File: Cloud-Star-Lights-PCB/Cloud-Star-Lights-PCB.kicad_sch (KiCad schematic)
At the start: 79 parts, among them U1 RP2040, U2 PCA9685PW, U3 PCA9685PW

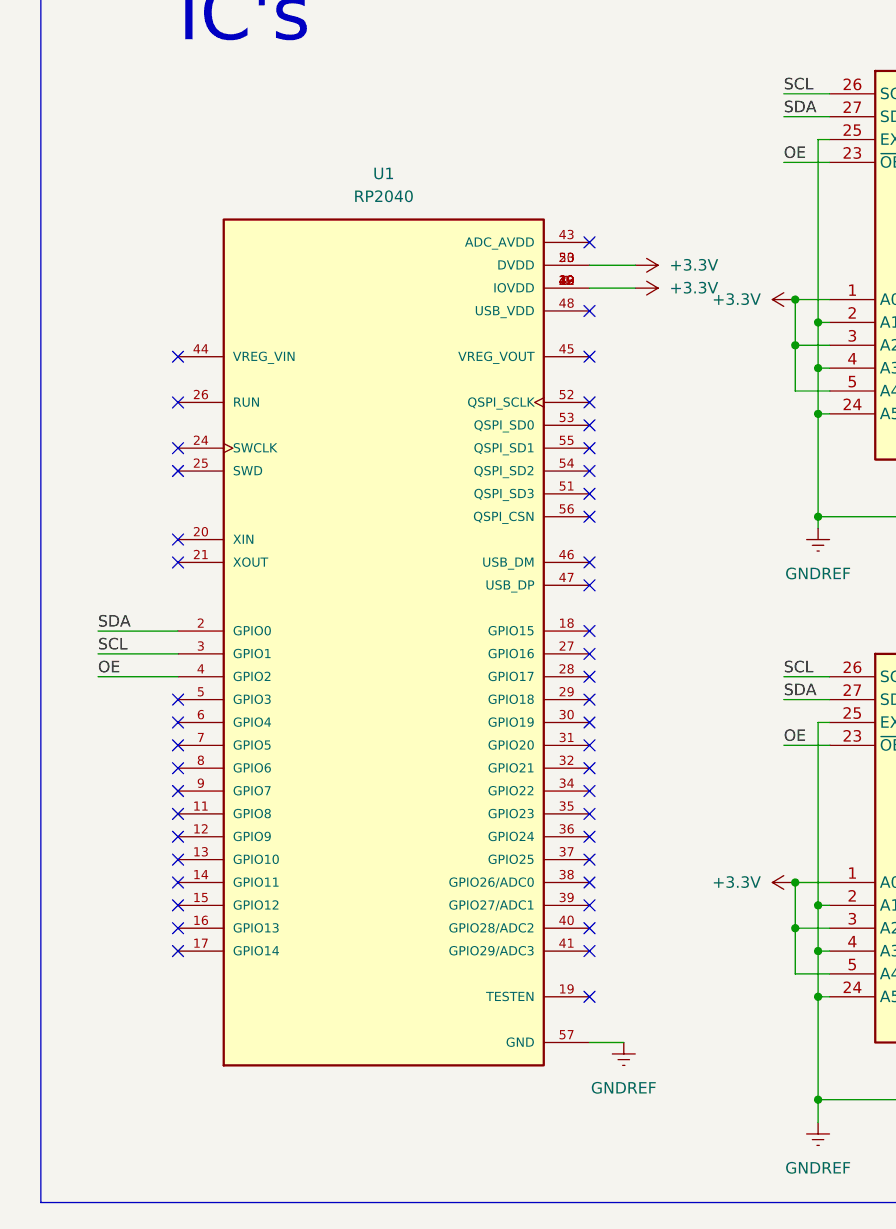
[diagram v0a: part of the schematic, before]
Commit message: Convert to ESP chip and localize library (hopefully)
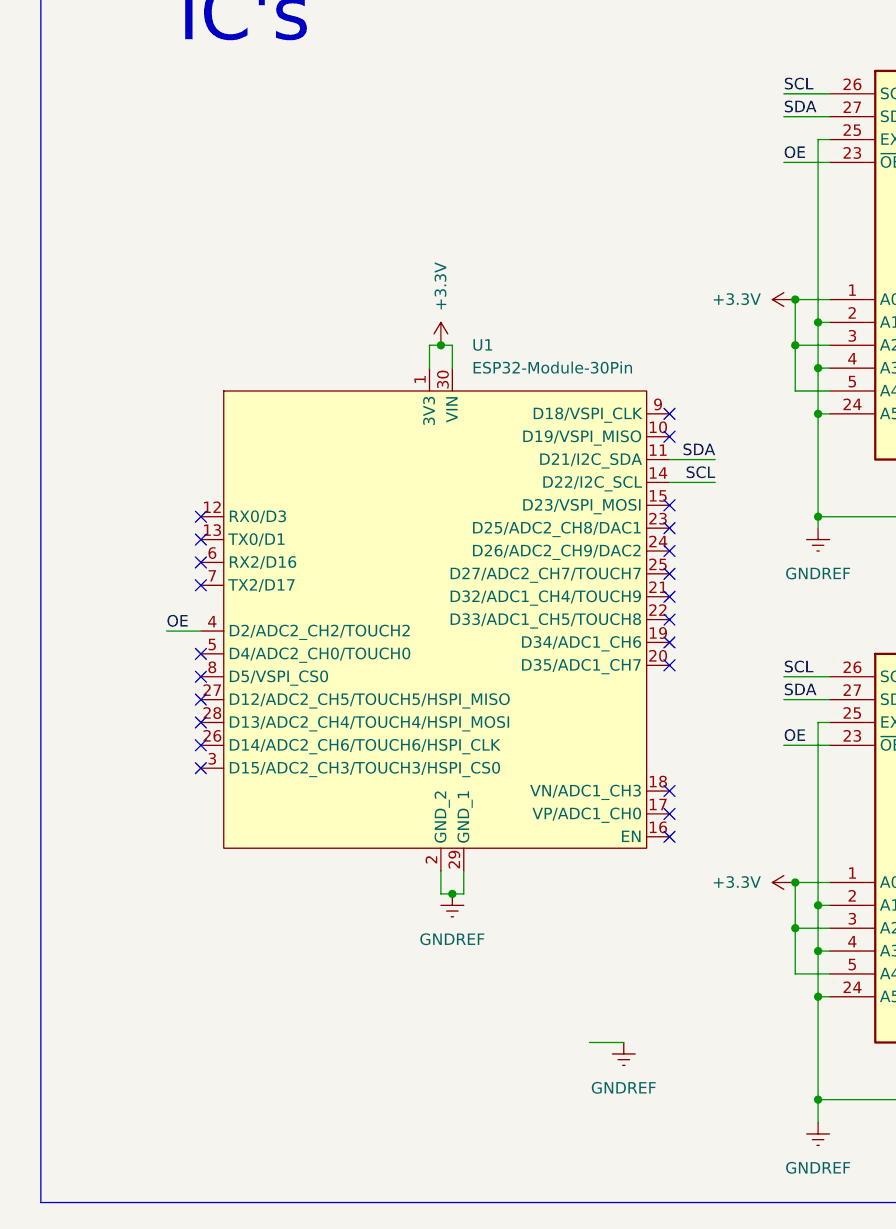
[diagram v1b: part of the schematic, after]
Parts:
- removed U1: RP2040, RP2040:QFN40P700X700X90-57N, symbol RP2040:RP2040
- added U1: ESP32-Module-30Pin, Project-Supernova-Footprint-Lib:ESP32-Module-30Pin, symbol Library:ESP32-Module-30Pin
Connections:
- net +3.3V: now also U1.1 (3V3), U1.30 (VIN)
- net GNDREF: now also U1.2 (GND_2), U1.29 (GND_1)
- net OE: now also U1.4 (D2/ADC2_CH2/TOUCH2)
- net SCL: now also U1.14 (D22/I2C_SCL)
- net SDA: now also U1.11 (D21/I2C_SDA)
- no-connect marks 47 -> 25

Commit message: Praying to god my library is right
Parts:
- J1, J10, J11, J12, J13, J14, J15, J16, J17, J18, J19, J2, J20, J21, J22, J23, J24, J25, J26, J27, J28, J29, J3, J30, J31, J32, J33, J34, J35, J36, J37, J38, J39, J4, J40, J41, J42, J43, J44, J45, J5, J6, J7, J8, J9: footprint (none) -> Library:0353120460
- J46: footprint (none) -> Library:Cixi_Kefa_Elec_KF135T-10.16-3P
- Q1, Q10, Q11, Q12, Q13, Q14, Q15, Q16, Q17, Q18, Q19, Q2, Q20, Q21, Q22, Q23, Q24, Q25, Q26, Q27, Q28, Q29, Q3, Q30, Q4, Q5, Q6, Q7, Q8, Q9: footprint (none) -> Library:AP5N10S
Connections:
- net OE: now also U1.15 (D23/VSPI_MOSI); no longer U1.4 (D2/ADC2_CH2/TOUCH2)

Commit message: Schematics Done
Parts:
- removed J1, J10, J11, J12, J13, J14, J15, J16, J17, J18, J19, J2, J20, J21, J22, J23, J24, J25, J26, J27, J28, J29, J3, J30, J31, J32, J33, J34, J35, J36, J37, J38, J39, J4, J40, J41, J42, J43, J44, J45, J5, J6, J7, J8, J9: ~, Library:0353120460, symbol Library:0353120460
- removed Q1, Q10, Q11, Q12, Q13, Q14, Q15, Q16, Q17, Q18, Q19, Q2, Q20, Q21, Q22, Q23, Q24, Q25, Q26, Q27, Q28, Q29, Q3, Q4, Q5, Q6, Q7, Q8, Q9: ~, Library:AP5N10S, symbol Library:AP5N10S
- added J1, J32, J33, J34, J35, J36, J37, J38, J39, J40, J41, J42, J43, J44, J45: ~, symbol Library:JILN_JL301-50004U01
- added J10, J11, J12, J13, J14, J15, J16, J17, J18, J19, J2, J20, J21, J22, J23, J24, J25, J26, J27, J28, J29, J3, J30, J31, J4, J5, J6, J7, J8, J9: ~, symbol Library:MAX_MX126-5.0-02P-GN01-Cu-S-A
- added Q1, Q10, Q11, Q12, Q13, Q14, Q15, Q16, Q17, Q18, Q19, Q2, Q20, Q21, Q22, Q23, Q24, Q25, Q26, Q27, Q28, Q29, Q3, Q31, Q4, Q5, Q6, Q7, Q8, Q9: 2N3906, Package_TO_SOT_THT:TO-92_Inline, symbol Transistor_BJT:2N3906
- added Q32, Q33, Q34, Q35, Q36, Q37, Q38, Q39, Q40, Q41, Q42, Q43, Q44, Q45, Q46, Q47, Q48, Q49, Q50, Q51, Q52, Q53, Q54, Q55, Q56, Q57, Q58, Q59, Q60, Q61, Q62, Q63, Q64, Q65, Q66, Q67, Q68, Q69, Q70, Q71, Q72, Q73, Q74, Q75: ~, Library:AP5N10S, symbol Library:AP5N10S
- added R1, R10, R11, R12, R13, R14, R15, R16, R17, R18, R19, R2, R20, R21, R22, R23, R24, R25, R26, R27, R28, R29, R3, R30, R4, R5, R6, R7, R8, R9: ~, Resistor_SMD:R_0201_0603Metric_Pad0.64x0.40mm_HandSolder, symbol Library:ERJP03J220V
- added U4: PCA9685PW, Package_SO:TSSOP-28_4.4x9.7mm_P0.65mm, symbol Driver_LED:PCA9685PW
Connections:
- net Stars_Power_B5 is gone; now on net Cloud_Control_R1: Q30.1 (B)
- net +3.3V: now also U4.1 (A0), U4.24 (A5), U4.28 (VDD), U4.3 (A2); no longer U3.5 (A4)
- net +5V: now also J1.4, J32.4, J33.4, J34.4, J35.4, J36.4, J37.4, J38.4, J39.4, J40.4, J41.4, J42.4, J43.4, J44.4, J45.4, Q1.1 (E), Q10.1 (E), Q11.1 (E), Q12.1 (E), Q13.1 (E), Q14.1 (E), Q15.1 (E), Q16.1 (E), Q17.1 (E), Q18.1 (E), Q19.1 (E), Q2.1 (E), Q20.1 (E), Q21.1 (E), Q22.1 (E), Q23.1 (E), Q24.1 (E), Q25.1 (E), Q26.1 (E), Q27.1 (E), Q28.1 (E), Q29.1 (E), Q3.1 (E), Q31.1 (E), Q4.1 (E), Q5.1 (E), Q6.1 (E), Q7.1 (E), Q8.1 (E), Q9.1 (E)
- net GNDREF: now also Q30.3 (E), U3.5 (A4), J10.2, J11.2, J12.2, J13.2, J14.2, J15.2, J16.2, J17.2, J18.2, J19.2, J2.2, J20.2, J21.2, J22.2, J23.2, J24.2, J25.2, J26.2, J27.2, J28.2, J29.2, J3.2, J30.2, J31.2, J4.2, J5.2, J6.2, J7.2, J8.2, J9.2, Q32.3 (E), Q33.3 (E), Q34.3 (E), Q35.3 (E), Q36.3 (E), Q37.3 (E), Q38.3 (E), Q39.3 (E), Q40.3 (E), Q41.3 (E), Q42.3 (E), Q43.3 (E), Q44.3 (E), Q45.3 (E), Q46.3 (E), Q47.3 (E), Q48.3 (E), Q49.3 (E), Q50.3 (E), Q51.3 (E), Q52.3 (E), Q53.3 (E), Q54.3 (E), Q55.3 (E), Q56.3 (E), Q57.3 (E), Q58.3 (E), Q59.3 (E), Q60.3 (E), Q61.3 (E), Q62.3 (E), Q63.3 (E), Q64.3 (E), Q65.3 (E), Q66.3 (E), Q67.3 (E), Q68.3 (E), Q69.3 (E), Q70.3 (E), Q71.3 (E), Q72.3 (E), Q73.3 (E), Q74.3 (E), Q75.3 (E), U4.14 (VSS), U4.2 (A1), U4.25 (EXTCLK), U4.4 (A3), U4.5 (A4); no longer Q30.1 (E)
- net OE: now also U4.23 (~{OE})
- net SCL: now also U4.26 (SCL)
- net SDA: now also U4.27 (SDA)
- net Clouds_Control_B1 renamed Star_Control_3
- net Star_Control_3: now also Q2.2 (B)
- net Clouds_Control_B2 renamed Star_Control_6
- net Star_Control_6: now also Q5.2 (B)
- net Clouds_Control_B3 renamed Star_Control_9
- net Star_Control_9: now also Q8.2 (B)
- net Clouds_Control_B4 renamed Star_Control_12
- net Star_Control_12: now also Q11.2 (B)
- net Clouds_Control_B5 renamed Star_Control_15
- net Star_Control_15: now also Q14.2 (B)
- net Clouds_Control_G1 renamed Star_Control_2
- net Star_Control_2: now also Q1.2 (B)
- net Clouds_Control_G2 renamed Star_Control_5
- net Star_Control_5: now also Q4.2 (B)
- net Clouds_Control_G3 renamed Star_Control_8
- net Star_Control_8: now also Q7.2 (B)
- net Clouds_Control_G4 renamed Star_Control_11
- net Star_Control_11: now also Q10.2 (B)
- net Clouds_Control_G5 renamed Star_Control_14
- net Star_Control_14: now also Q13.2 (B)
- net Clouds_Control_R1 renamed Star_Control_1
- net Star_Control_1: now also Q31.2 (B)
- net Clouds_Control_R2 renamed Star_Control_4
- net Star_Control_4: now also Q3.2 (B)
- net Clouds_Control_R3 renamed Star_Control_7
- net Star_Control_7: now also Q6.2 (B)
- net Clouds_Control_R4 renamed Star_Control_10
- net Star_Control_10: now also Q9.2 (B)
- net Clouds_Control_R5 renamed Star_Control_13
- net Star_Control_13: now also Q12.2 (B)
- net Stars_Control_B1 renamed Star_Control_18
- net Star_Control_18: now also Q17.2 (B)
- net Stars_Control_B2 renamed Star_Control_21
- net Star_Control_21: now also Q20.2 (B)
- net Stars_Control_B3 renamed Star_Control_24
- net Star_Control_24: now also Q23.2 (B)
- net Stars_Control_B4 renamed Star_Control_27
- net Star_Control_27: now also Q26.2 (B)
- net Stars_Control_B5 renamed Cloud_Control_R1
- net Cloud_Control_R1: now also Q34.1 (B), Q37.1 (B), U4.6 (LED0); no longer U3.21 (LED14)
- net Stars_Control_G1 renamed Star_Control_17
- net Star_Control_17: now also Q16.2 (B)
- net Stars_Control_G2 renamed Star_Control_20
- net Star_Control_20: now also Q19.2 (B)
- net Stars_Control_G3 renamed Star_Control_23
- net Star_Control_23: now also Q22.2 (B)
- net Stars_Control_G4 renamed Star_Control_26
- net Star_Control_26: now also Q25.2 (B)
- net Stars_Control_G5 renamed Star_Control_29
- net Star_Control_29: now also Q28.2 (B)
- net Stars_Control_R1 renamed Star_Control_16
- net Star_Control_16: now also Q15.2 (B)
- net Stars_Control_R2 renamed Star_Control_19
- net Star_Control_19: now also Q18.2 (B)
- net Stars_Control_R3 renamed Star_Control_22
- net Star_Control_22: now also Q21.2 (B)
- net Stars_Control_R4 renamed Star_Control_25
- net Star_Control_25: now also Q24.2 (B)
- net Stars_Control_R5 renamed Star_Control_28
- net Star_Control_28: now also Q27.2 (B)
- new net: J41.1, Q61.2 (C)
- new net: J41.2, Q62.2 (C)
- new net: J41.3, Q63.2 (C)
- new net: J2.1, R1.2
- new net: Q14.3 (C), R15.1
- new net: J16.1, R15.2
- new net: J43.1, Q67.2 (C)
- new net: J43.2, Q68.2 (C)
- new net: J43.3, Q69.2 (C)
- new net: Q13.3 (C), R14.1
- new net: J15.1, R14.2
- new net: J37.1, Q49.2 (C)
- new net: Q19.3 (C), R20.1
- new net: J21.1, R20.2
- new net: J37.3, Q51.2 (C)
- new net: Q2.3 (C), R3.1
- new net: J4.1, R3.2
- new net: Q29.3 (C), R30.1
- new net: J31.1, R30.2
- new net: Q18.3 (C), R19.1
- new net: J20.1, R19.2
- new net: J22.1, R21.2
- new net: J25.1, R24.2
- new net: Q21.3 (C), R22.1
- new net: J23.1, R22.2
- new net: J18.1, R17.2
- new net: J13.1, R12.2
- new net: Q20.3 (C), R21.1
- new net: Q28.3 (C), R29.1
- new net: J42.2, Q65.2 (C)
- new net: Q26.3 (C), R27.1
- new net: J28.1, R27.2
- new net: Q16.3 (C), R17.1
- new net: J35.1, Q43.2 (C)
- new net: J32.3, Q36.2 (C)
- new net: J34.1, Q40.2 (C)
- new net: J39.1, Q55.2 (C)
- new net: J39.2, Q56.2 (C)
- new net: J39.3, Q57.2 (C)
- new net: Q10.3 (C), R11.1
- new net: J12.1, R11.2
- new net: Q1.3 (C), R2.1
- new net: J3.1, R2.2
- new net: J37.2, Q50.2 (C)
- new net: J14.1, R13.2
- new net: J5.1, R4.2
- new net: J1.2, Q32.2 (C)
- new net: J32.1, Q34.2 (C)
- new net: J32.2, Q35.2 (C)
- new net: Q15.3 (C), R16.1
- new net: Q7.3 (C), R8.1
- new net: J9.1, R8.2
- new net: J33.2, Q38.2 (C)
- new net: J8.1, R7.2
- new net: J33.1, Q37.2 (C)
- new net: J33.3, Q39.2 (C)
- new net: J27.1, R26.2
- new net: Q12.3 (C), R13.1
- new net: J34.3, Q42.2 (C)
- new net: J44.2, Q71.2 (C)
- new net: J38.2, Q53.2 (C)
- new net: Q4.3 (C), R5.1
- new net: Q5.3 (C), R6.1
- new net: J38.3, Q54.2 (C)
- new net: J45.1, Q73.2 (C)
- new net: J45.2, Q74.2 (C)
- new net: J45.3, Q75.2 (C)
- new net: Q11.3 (C), R12.1
- new net: J6.1, R5.2
- new net: J38.1, Q52.2 (C)
- new net: Q22.3 (C), R23.1
- new net: J24.1, R23.2
- new net: Q9.3 (C), R10.1
- new net: J36.2, Q47.2 (C)
- new net: J19.1, R18.2
- new net: J30.1, R29.2
- new net: J40.2, Q59.2 (C)
- new net: Q17.3 (C), R18.1
- new net: J35.3, Q45.2 (C)
- new net: J42.3, Q66.2 (C)
- new net: Q8.3 (C), R9.1
- new net: J10.1, R9.2
- new net: J17.1, R16.2
- new net: J44.1, Q70.2 (C)
- new net: J34.2, Q41.2 (C)
- new net: J1.3, Q33.2 (C)
- new net: Q27.3 (C), R28.1
- new net: J29.1, R28.2
- new net: Q3.3 (C), R4.1
- new net: J26.1, R25.2
- new net: Q24.3 (C), R25.1
- new net: J35.2, Q44.2 (C)
- new net: Q6.3 (C), R7.1
- new net: J40.1, Q58.2 (C)
- new net: J40.3, Q60.2 (C)
- new net: Q31.3 (C), R1.1
- new net: J7.1, R6.2
- new net: Q25.3 (C), R26.1
- new net: Q23.3 (C), R24.1
- new net: J1.1, Q30.2 (C)
- new net: J42.1, Q64.2 (C)
- new net: J11.1, R10.2
- new net: J36.3, Q48.2 (C)
- new net: J36.1, Q46.2 (C)
- new net: J44.3, Q72.2 (C)
- new net Cloud_Control_B1: Q33.1 (B), Q36.1 (B), Q39.1 (B), U4.17 (LED10)
- new net Cloud_Control_B2: Q42.1 (B), Q54.1 (B), Q66.1 (B), U4.18 (LED11)
- new net Cloud_Control_B3: Q45.1 (B), Q57.1 (B), Q69.1 (B), U4.19 (LED12)
- new net Cloud_Control_B4: Q48.1 (B), Q60.1 (B), Q72.1 (B), U4.20 (LED13)
- new net Cloud_Control_B5: Q51.1 (B), Q63.1 (B), Q75.1 (B), U4.21 (LED14)
- new net Cloud_Control_G1: Q32.1 (B), Q35.1 (B), Q38.1 (B), U4.11 (LED5)
- new net Cloud_Control_G2: Q41.1 (B), Q53.1 (B), Q65.1 (B), U4.12 (LED6)
- new net Cloud_Control_G3: Q44.1 (B), Q56.1 (B), Q68.1 (B), U4.13 (LED7)
- new net Cloud_Control_G4: Q47.1 (B), Q59.1 (B), Q71.1 (B), U4.15 (LED8)
- new net Cloud_Control_G5: Q50.1 (B), Q62.1 (B), Q74.1 (B), U4.16 (LED9)
- new net Cloud_Control_R2: Q40.1 (B), Q52.1 (B), Q64.1 (B), U4.7 (LED1)
- new net Cloud_Control_R3: Q43.1 (B), Q55.1 (B), Q67.1 (B), U4.8 (LED2)
- new net Cloud_Control_R4: Q46.1 (B), Q58.1 (B), Q70.1 (B), U4.9 (LED3)
- new net Cloud_Control_R5: Q49.1 (B), Q61.1 (B), Q73.1 (B), U4.10 (LED4)
- new net Star_Control_30: Q29.2 (B), U3.21 (LED14)
- no-connect marks 25 -> 26
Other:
- note added: "Clound Control"
- note added: "Star Control"
- note removed: "LEDs have 3 channels: Red, Green, Blue 50mA per 10cm per channel of LEDs Clouds have 60cm -> 300mA per channel Stars have 30cm -> 150mA per channel Group stars and clouds into 5 groups each -> 3 clouds per group, so 0.9A per channel per group -> 6 stars per group, so 0.9A per channel per group Each channel group transistor needs: -> Equal to or above 5V drain source voltage -> Equal to or above 0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"
- note removed: "Off Board Connections"
- note removed: "Transistors (NPN)"
- moved on the sheet: J46

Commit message: Comments
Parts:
- removed R1, R10, R11, R12, R13, R14, R15, R16, R17, R18, R19, R2, R20, R21, R22, R23, R24, R25, R26, R27, R28, R29, R3, R30, R4, R5, R6, R7, R8, R9: ~, Resistor_SMD:R_0201_0603Metric_Pad0.64x0.40mm_HandSolder, symbol Library:ERJP03J220V
- removed U2, U3, U4: PCA9685PW, Package_SO:TSSOP-28_4.4x9.7mm_P0.65mm, symbol Driver_LED:PCA9685PW
- added C1: C, symbol Device:C
- added J31, J32, J49: ~, Library:MAX_MX126-5.0-02P-GN01-Cu-S-A, symbol Library:MAX_MX126-5.0-02P-GN01-Cu-S-A
- added R1, R10, R11, R12, R13, R14, R15, R16, R17, R18, R19, R2, R20, R21, R22, R23, R24, R25, R26, R27, R28, R29, R3, R30, R4, R5, R6, R7, R8, R9: 22Ω, Resistor_SMD:R_0201_0603Metric_Pad0.64x0.40mm_HandSolder, symbol Device:R
- added U1, U3, U4: ~, symbol Library:PCA9685_Breakout
- J1: renamed from J2; footprint (none) -> Library:MAX_MX126-5.0-02P-GN01-Cu-S-A
- J10: renamed from J11; footprint (none) -> Library:MAX_MX126-5.0-02P-GN01-Cu-S-A
- J11: renamed from J12; footprint (none) -> Library:MAX_MX126-5.0-02P-GN01-Cu-S-A
- J12: renamed from J13; footprint (none) -> Library:MAX_MX126-5.0-02P-GN01-Cu-S-A
- J13: renamed from J14; footprint (none) -> Library:MAX_MX126-5.0-02P-GN01-Cu-S-A
- J14: renamed from J15; footprint (none) -> Library:MAX_MX126-5.0-02P-GN01-Cu-S-A
- J15: renamed from J16; footprint (none) -> Library:MAX_MX126-5.0-02P-GN01-Cu-S-A
- J16: renamed from J17; footprint (none) -> Library:MAX_MX126-5.0-02P-GN01-Cu-S-A
- J17: renamed from J18; footprint (none) -> Library:MAX_MX126-5.0-02P-GN01-Cu-S-A
- J18: renamed from J19; footprint (none) -> Library:MAX_MX126-5.0-02P-GN01-Cu-S-A
- J19: renamed from J20; footprint (none) -> Library:MAX_MX126-5.0-02P-GN01-Cu-S-A
- J2: renamed from J3; footprint (none) -> Library:MAX_MX126-5.0-02P-GN01-Cu-S-A
- J20: renamed from J21; footprint (none) -> Library:MAX_MX126-5.0-02P-GN01-Cu-S-A
- J21: renamed from J22; footprint (none) -> Library:MAX_MX126-5.0-02P-GN01-Cu-S-A
- J22: renamed from J23; footprint (none) -> Library:MAX_MX126-5.0-02P-GN01-Cu-S-A
- J23: renamed from J24; footprint (none) -> Library:MAX_MX126-5.0-02P-GN01-Cu-S-A
- J24: renamed from J25; footprint (none) -> Library:MAX_MX126-5.0-02P-GN01-Cu-S-A
- J25: renamed from J26; footprint (none) -> Library:MAX_MX126-5.0-02P-GN01-Cu-S-A
- J26: renamed from J27; footprint (none) -> Library:MAX_MX126-5.0-02P-GN01-Cu-S-A
- J27: renamed from J28; footprint (none) -> Library:MAX_MX126-5.0-02P-GN01-Cu-S-A
- J28: renamed from J29; footprint (none) -> Library:MAX_MX126-5.0-02P-GN01-Cu-S-A
- J29: renamed from J30; footprint (none) -> Library:MAX_MX126-5.0-02P-GN01-Cu-S-A
- J3: renamed from J4; footprint (none) -> Library:MAX_MX126-5.0-02P-GN01-Cu-S-A
- J30: renamed from J31; footprint (none) -> Library:MAX_MX126-5.0-02P-GN01-Cu-S-A
- J34: renamed from J1; footprint (none) -> Library:JILN_JL301-50004U01
- J35: renamed from J34; footprint (none) -> Library:JILN_JL301-50004U01
- J36: renamed from J35; footprint (none) -> Library:JILN_JL301-50004U01
- J37: renamed from J36; footprint (none) -> Library:JILN_JL301-50004U01
- J38: renamed from J37; footprint (none) -> Library:JILN_JL301-50004U01
- J39: renamed from J32; footprint (none) -> Library:JILN_JL301-50004U01
- J4: renamed from J5; footprint (none) -> Library:MAX_MX126-5.0-02P-GN01-Cu-S-A
- J40: renamed from J38; footprint (none) -> Library:JILN_JL301-50004U01
- J41: renamed from J39; footprint (none) -> Library:JILN_JL301-50004U01
- J42: renamed from J40; footprint (none) -> Library:JILN_JL301-50004U01
- J43: renamed from J41; footprint (none) -> Library:JILN_JL301-50004U01
- J44: renamed from J33; footprint (none) -> Library:JILN_JL301-50004U01
- J45: renamed from J42; footprint (none) -> Library:JILN_JL301-50004U01
- J46: renamed from J43; footprint (none) -> Library:JILN_JL301-50004U01
- J47: renamed from J44; footprint (none) -> Library:JILN_JL301-50004U01
- J48: renamed from J45; footprint (none) -> Library:JILN_JL301-50004U01
- J5: renamed from J6; footprint (none) -> Library:MAX_MX126-5.0-02P-GN01-Cu-S-A
- J6: renamed from J7; footprint (none) -> Library:MAX_MX126-5.0-02P-GN01-Cu-S-A
- J7: renamed from J8; footprint (none) -> Library:MAX_MX126-5.0-02P-GN01-Cu-S-A
- J8: renamed from J9; footprint (none) -> Library:MAX_MX126-5.0-02P-GN01-Cu-S-A
- J9: renamed from J10; footprint (none) -> Library:MAX_MX126-5.0-02P-GN01-Cu-S-A
- U2: renamed from U1; footprint Project-Supernova-Footprint-Lib:ESP32-Module-30Pin -> Library:ESP32-Module-30Pin
- renumbered J46 to J33, Q31 to Q1, Q9 to Q10, Q10 to Q11, Q11 to Q12, Q12 to Q13, Q13 to Q14, Q14 to Q15, Q15 to Q16, Q16 to Q17, Q17 to Q18, Q18 to Q19, Q1 to Q2, Q19 to Q20, Q20 to Q21, Q21 to Q22, Q22 to Q23, Q23 to Q24, Q24 to Q25, Q25 to Q26, Q26 to Q27, Q27 to Q28, Q28 to Q29, Q2 to Q3, Q29 to Q30, Q30 to Q31, Q40 to Q32, Q43 to Q33, Q46 to Q34, Q49 to Q35, Q32 to Q36, Q41 to Q37, Q44 to Q38, Q47 to Q39, Q3 to Q4, Q50 to Q40, Q33 to Q41, Q45 to Q43, Q48 to Q44, Q51 to Q45, Q34 to Q46, Q52 to Q47, Q55 to Q48, Q58 to Q49, Q4 to Q5, Q61 to Q50, Q35 to Q51, Q53 to Q52, Q56 to Q53, Q59 to Q54, Q62 to Q55, Q36 to Q56, Q54 to Q57, Q57 to Q58, Q60 to Q59, Q5 to Q6, Q63 to Q60, Q37 to Q61, Q64 to Q62, Q67 to Q63, Q70 to Q64, Q73 to Q65, Q38 to Q66, Q65 to Q67, Q71 to Q69, Q6 to Q7, Q74 to Q70, Q39 to Q71, Q66 to Q72, Q69 to Q73, Q72 to Q74, Q7 to Q8, Q8 to Q9
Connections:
- net +3.3V: now also J32.1, U1.5 (VCC), U3.5 (VCC), U4.5 (VCC)
- net +5V: no longer Q26.1 (E)
- net Cloud_Control_B1: now also U4.16 (LED10)
- net Cloud_Control_B2: now also U4.17 (LED11)
- net Cloud_Control_B3: now also U4.18 (LED12)
- net Cloud_Control_B4: now also U4.19 (LED13)
- net Cloud_Control_B5: now also U4.20 (LED14)
- net Cloud_Control_G1: now also U4.11 (LED5)
- net Cloud_Control_G2: now also U4.12 (LED6)
- net Cloud_Control_G3: now also U4.13 (LED7)
- net Cloud_Control_G4: now also U4.14 (LED8)
- net Cloud_Control_G5: now also U4.15 (LED9)
- net Cloud_Control_R1: now also U4.6 (LED0)
- net Cloud_Control_R2: now also U4.7 (LED1)
- net Cloud_Control_R3: now also U4.8 (LED2)
- net Cloud_Control_R4: now also U4.9 (LED3)
- net Cloud_Control_R5: now also U4.10 (LED4)
- net GNDREF: no longer J1.2, J10.2, J11.2, J12.2, J13.2, J14.2, J15.2, J16.2, J17.2, J18.2, J19.2, J2.2, J20.2, J21.2, J22.2, J23.2, J24.2, J25.2, J26.2, J27.2, J28.2, J29.2, J3.2, J30.2, J33.3, J4.2, J5.2, J6.2, J7.2, J8.2, J9.2, U2.2 (GND_2), U2.29 (GND_1)
- net SCL: now also J49.2, U1.3 (SCL), U3.3 (SCL), U4.3 (SCL)
- net SDA: now also J49.1, U1.4 (SDA), U3.4 (SDA), U4.4 (SDA)
- net Star_Control_1: now also U1.6 (LED0)
- net Star_Control_10: now also U1.15 (LED9)
- net Star_Control_11: now also U1.16 (LED10)
- net Star_Control_12: now also U1.17 (LED11)
- net Star_Control_13: now also U1.18 (LED12)
- net Star_Control_14: now also U1.19 (LED13)
- net Star_Control_15: now also U1.20 (LED14)
- net Star_Control_16: now also U3.6 (LED0)
- net Star_Control_17: now also U3.7 (LED1)
- net Star_Control_18: now also U3.8 (LED2)
- net Star_Control_19: now also U3.9 (LED3)
- net Star_Control_2: now also U1.7 (LED1)
- net Star_Control_20: now also U3.10 (LED4)
- net Star_Control_21: now also U3.11 (LED5)
- net Star_Control_22: now also U3.12 (LED6)
- net Star_Control_23: now also U3.13 (LED7)
- net Star_Control_24: now also U3.14 (LED8)
- net Star_Control_25: now also U3.15 (LED9)
- net Star_Control_26: now also U3.16 (LED10)
- net Star_Control_27: now also U3.17 (LED11)
- net Star_Control_28: now also U3.18 (LED12)
- net Star_Control_29: now also U3.19 (LED13)
- net Star_Control_3: now also U1.8 (LED2)
- net Star_Control_30: now also U3.20 (LED14)
- net Star_Control_4: now also U1.9 (LED3)
- net Star_Control_5: now also U1.10 (LED4)
- net Star_Control_6: now also U1.11 (LED5)
- net Star_Control_7: now also U1.12 (LED6)
- net Star_Control_8: now also U1.13 (LED7)
- net Star_Control_9: now also U1.14 (LED8)
- net at J1.1: now also R1.2
- net at Q15.3 (C): now also R15.1
- net at J15.1: now also R15.2
- net at Q14.3 (C): now also R14.1
- net at J14.1: now also R14.2
- net at Q20.3 (C): now also R20.1
- net at J20.1: now also R20.2
- net at Q3.3 (C): now also R3.1
- net at J3.1: now also R3.2
- net at Q30.3 (C): now also R30.1
- net at J30.1: now also R30.2
- net at Q19.3 (C): now also R19.1
- net at J19.1: now also R19.2
- net at J21.1: now also R21.2
- net at J24.1: now also R24.2
- net at Q22.3 (C): now also R22.1
- net at J22.1: now also R22.2
- net at J17.1: now also R17.2
- net at J12.1: now also R12.2
- net at Q21.3 (C): now also R21.1
- net at Q29.3 (C): now also R29.1
- net at Q27.3 (C): now also R27.1
- net at J27.1: now also R27.2
- net at Q17.3 (C): now also R17.1
- net at Q11.3 (C): now also R11.1
- net at J11.1: now also R11.2
- net at Q2.3 (C): now also R2.1
- net at J2.1: now also R2.2
- net at J13.1: now also R13.2
- net at J4.1: now also R4.2
- net at Q16.3 (C): now also R16.1
- net at Q8.3 (C): now also R8.1
- net at J8.1: now also R8.2
- net at J7.1: now also R7.2
- net at J26.1: now also R26.2
- net at Q13.3 (C): now also R13.1
- net at Q5.3 (C): now also R5.1
- net at Q6.3 (C): now also R6.1
- net at Q12.3 (C): now also R12.1
- net at J5.1: now also R5.2
- net at Q23.3 (C): now also R23.1
- net at J23.1: now also R23.2
- net at Q10.3 (C): now also R10.1
- net at J18.1: now also R18.2
- net at J29.1: now also R29.2
- net at Q18.3 (C): now also R18.1
- net at Q9.3 (C): now also R9.1
- net at J9.1: now also R9.2
- net at J16.1: now also R16.2
- net at Q28.3 (C): now also R28.1
- net at J28.1: now also R28.2
- net at Q4.3 (C): now also R4.1
- net at J25.1: now also R25.2
- net at Q25.3 (C): now also R25.1
- net at Q7.3 (C): now also R7.1
- net at Q1.3 (C): now also R1.1
- net at J6.1: now also R6.2
- net at Q26.3 (C): now also R26.1
- net at Q24.3 (C): now also R24.1
- net at U2.16 (EN): now also C1.2
- net at J10.1: now also R10.2
- new net GND: C1.1, J1.2, J10.2, J11.2, J12.2, J13.2, J14.2, J15.2, J16.2, J17.2, J18.2, J19.2, J2.2, J20.2, J21.2, J22.2, J23.2, J24.2, J25.2, J26.2, J27.2, J28.2, J29.2, J3.2, J30.2, J31.1, J31.2, J32.2, J33.3, J4.2, J5.2, J6.2, J7.2, J8.2, J9.2, U1.1 (GND), U2.2 (GND_2), U2.29 (GND_1), U3.1 (GND), U4.1 (GND)
- new net Output_Enable: U1.2 (OE), U3.2 (OE), U4.2 (OE)
- no-connect marks 26 -> 25
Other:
- note added: "30 LED's per meter Cut lines every 10cm 50mA/10cm -> 5mA/cm per channel Clouds have 60cm -> 300mA / 0.3A per channel 0.3A * 5v = 1.5W per LED LED lines have a common power Thus transistor on opposite side compared to the star config"
- note added: "30 Stars 0.625W / 0.11WperLED = 5 LED max per board 3 LED's per board * 0.05A per LED = 0.15A for the board V = IR (5V - 2.15V) = 0.15A * R R = 2.85V / 0.15A R = 19ohm = 22ohm Transistor could be put on either side, I think it's cleaner being right before the resistor"
- moved on the sheet: J33

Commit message: Schematic changes
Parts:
- removed J1, J10, J11, J12, J13, J14, J15, J16, J17, J18, J19, J2, J20, J21, J22, J23, J24, J25, J26, J27, J28, J29, J3, J30, J31, J32, J4, J49, J5, J6, J7, J8, J9: ~, Library:MAX_MX126-5.0-02P-GN01-Cu-S-A, symbol Library:MAX_MX126-5.0-02P-GN01-Cu-S-A
- removed J33: ~, Library:Cixi_Kefa_Elec_KF135T-10.16-3P, symbol Library:Cixi_Kefa_Elec_KF135T-10.16-3P
- removed J34, J35, J36, J37, J38, J39, J40, J41, J42, J43, J44, J45, J46, J47, J48: ~, Library:JILN_JL301-50004U01, symbol Library:JILN_JL301-50004U01
- added J1, J10, J11, J12, J13, J14, J15, J16, J17, J18, J19, J2, J20, J21, J22, J23, J24, J25, J26, J27, J28, J29, J3, J30, J4, J46, J47, J48, J5, J6, J7, J8, J9: Conn_01x02, symbol Connector_Generic:Conn_01x02
- added J31, J32, J33, J34, J35, J36, J37, J38, J39, J40, J41, J42, J43, J44, J45: Conn_01x04, symbol Connector_Generic:Conn_01x04
- added J49: Conn_01x03, symbol Connector_Generic:Conn_01x03
- C1: value C -> 0.1uF; now not fitted
- U1, U3, U4: value ~ -> PCA9685 Breakout
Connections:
- net Output_Enable is gone; now on net OUTPUT_ENABLE: U1.2 (OE), U3.2 (OE), U4.2 (OE)
- net +3.3V: now also J48.1 (Pin_1), J49.1 (Pin_1)
- net +5V: now also J31.4 (Pin_4), J32.4 (Pin_4), J33.4 (Pin_4), J34.4 (Pin_4), J35.4 (Pin_4), J36.4 (Pin_4), J37.4 (Pin_4), J38.4 (Pin_4), J39.4 (Pin_4), J40.4 (Pin_4), J41.4 (Pin_4), J42.4 (Pin_4), J43.4 (Pin_4), J44.4 (Pin_4), J45.4 (Pin_4), J49.2 (Pin_2)
- net GND: now also J1.2 (Pin_2), J10.2 (Pin_2), J11.2 (Pin_2), J12.2 (Pin_2), J13.2 (Pin_2), J14.2 (Pin_2), J15.2 (Pin_2), J16.2 (Pin_2), J17.2 (Pin_2), J18.2 (Pin_2), J19.2 (Pin_2), J2.2 (Pin_2), J20.2 (Pin_2), J21.2 (Pin_2), J22.2 (Pin_2), J23.2 (Pin_2), J24.2 (Pin_2), J25.2 (Pin_2), J26.2 (Pin_2), J27.2 (Pin_2), J28.2 (Pin_2), J29.2 (Pin_2), J3.2 (Pin_2), J30.2 (Pin_2), J4.2 (Pin_2), J47.1 (Pin_1), J47.2 (Pin_2), J48.2 (Pin_2), J49.3 (Pin_3), J5.2 (Pin_2), J6.2 (Pin_2), J7.2 (Pin_2), J8.2 (Pin_2), J9.2 (Pin_2)
- net SCL: now also J46.2 (Pin_2)
- net SDA: now also J46.1 (Pin_1)
- net at Q50.2 (S): now also J40.1 (Pin_1)
- net at Q55.2 (S): now also J40.2 (Pin_2)
- net at Q60.2 (S): now also J40.3 (Pin_3)
- net at R1.2: now also J1.1 (Pin_1)
- net at Q63.2 (S): now also J43.1 (Pin_1)
- net at Q68.2 (S): now also J43.2 (Pin_2)
- net at Q73.2 (S): now also J43.3 (Pin_3)
- net at Q35.2 (S): now also J35.1 (Pin_1)
- net at Q45.2 (S): now also J35.3 (Pin_3)
- net at R21.2: now also J21.1 (Pin_1)
- net at R24.2: now also J24.1 (Pin_1)
- net at R17.2: now also J17.1 (Pin_1)
- net at R12.2: now also J12.1 (Pin_1)
- net at R13.2: now also J13.1 (Pin_1)
- net at Q67.2 (S): now also J42.2 (Pin_2)
- net at Q33.2 (S): now also J33.1 (Pin_1)
- net at R2.2: now also J2.1 (Pin_1)
- net at Q56.2 (S): now also J36.3 (Pin_3)
- net at Q32.2 (S): now also J32.1 (Pin_1)
- net at Q48.2 (S): now also J38.1 (Pin_1)
- net at Q53.2 (S): now also J38.2 (Pin_2)
- net at Q58.2 (S): now also J38.3 (Pin_3)
- net at Q40.2 (S): now also J35.2 (Pin_2)
- net at R4.2: now also J4.1 (Pin_1)
- net at R28.2: now also J28.1 (Pin_1)
- net at Q36.2 (S): now also J31.2 (Pin_2)
- net at Q46.2 (S): now also J36.1 (Pin_1)
- net at Q51.2 (S): now also J36.2 (Pin_2)
- net at R19.2: now also J19.1 (Pin_1)
- net at Q66.2 (S): now also J41.2 (Pin_2)
- net at R7.2: now also J7.1 (Pin_1)
- net at Q61.2 (S): now also J41.1 (Pin_1)
- net at Q71.2 (S): now also J41.3 (Pin_3)
- net at R15.2: now also J15.1 (Pin_1)
- net at R26.2: now also J26.1 (Pin_1)
- net at R8.2: now also J8.1 (Pin_1)
- net at R25.2: now also J25.1 (Pin_1)
- net at Q42.2 (S): now also J32.3 (Pin_3)
- net at Q69.2 (S): now also J44.2 (Pin_2)
- net at Q52.2 (S): now also J37.2 (Pin_2)
- net at Q57.2 (S): now also J37.3 (Pin_3)
- net at Q65.2 (S): now also J45.1 (Pin_1)
- net at Q70.2 (S): now also J45.2 (Pin_2)
- net at Q75.2 (S): now also J45.3 (Pin_3)
- net at Q47.2 (S): now also J37.1 (Pin_1)
- net at R6.2: now also J6.1 (Pin_1)
- net at Q39.2 (S): now also J34.2 (Pin_2)
- net at R29.2: now also J29.1 (Pin_1)
- net at R18.2: now also J18.1 (Pin_1)
- net at Q54.2 (S): now also J39.2 (Pin_2)
- net at R23.2: now also J23.1 (Pin_1)
- net at R5.2: now also J5.1 (Pin_1)
- net at Q43.2 (S): now also J33.3 (Pin_3)
- net at Q72.2 (S): now also J42.3 (Pin_3)
- net at R11.2: now also J11.1 (Pin_1)
- net at R30.2: now also J30.1 (Pin_1)
- net at Q64.2 (S): now also J44.1 (Pin_1)
- net at Q37.2 (S): now also J32.2 (Pin_2)
- net at Q41.2 (S): now also J31.3 (Pin_3)
- net at R14.2: now also J14.1 (Pin_1)
- net at Q38.2 (S): now also J33.2 (Pin_2)
- net at R20.2: now also J20.1 (Pin_1)
- net at Q49.2 (S): now also J39.1 (Pin_1)
- net at Q59.2 (S): now also J39.3 (Pin_3)
- net at R16.2: now also J16.1 (Pin_1)
- net at R9.2: now also J9.1 (Pin_1)
- net at R22.2: now also J22.1 (Pin_1)
- net at Q31.2 (S): now also J31.1 (Pin_1)
- net at Q62.2 (S): now also J42.1 (Pin_1)
- net at R10.2: now also J10.1 (Pin_1)
- net at R3.2: now also J3.1 (Pin_1)
- net at R27.2: now also J27.1 (Pin_1)
- net at Q44.2 (S): now also J34.3 (Pin_3)
- net at Q34.2 (S): now also J34.1 (Pin_1)
- net at Q74.2 (S): now also J44.3 (Pin_3)
- net OE renamed OUTPUT_ENABLE
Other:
- note added: "Cloud Control"
- note removed: "Clound Control"
- moved on the sheet: Q10, Q12, Q13, Q14, Q15, Q17, Q18, Q19, Q2, Q20, Q22, Q23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
